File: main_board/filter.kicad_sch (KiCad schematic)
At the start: 1 part

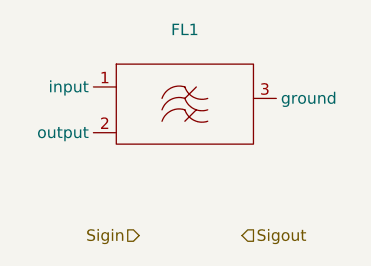
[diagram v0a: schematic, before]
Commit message: Revert "created band pass filter symbol and circuit."
This reverts commit e2b2576e5cedd48076742566f8c9abdfc840a111.

Remove bad commit
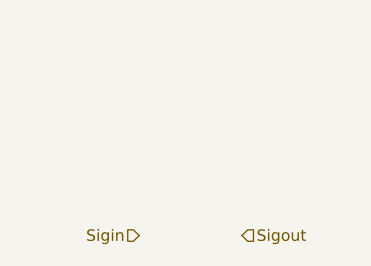
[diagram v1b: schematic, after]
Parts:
- removed FL1: ~, symbol bp_filter:457k_bandpass_filter
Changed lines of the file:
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@@
-		)
-	)
-	(symbol
-		(lib_id "bp_filter:457k_bandpass_filter")
-		(at 48.26 99.06 0)
-		(unit 1)
-		(exclude_from_sim no)
-		(in_bom yes)
-		(on_board yes)
-		(dnp no)
-		(fields_autoplaced yes)
-		(property "Reference" "FL1"
-			(at 48.26 85.09 0)
-			(effects
-				(font
-					(size 1.27 1.27)
-				)
-			)
-		)
-		(property "Value" "~"
-			(at 48.26 87.63 0)
-			(effects
-				(font
-					(size 1.27 1.27)
-				)
-			)
-		)
-		(property "Footprint" ""
-			(at 48.26 99.06 0)
-			(effects
-				(font
-					(size 1.27 1.27)
-				)
-				(hide yes)
-			)
-		)
-		(property "Datasheet" ""
-			(at 48.26 99.06 0)
-			(effects
-				(font
-					(size 1.27 1.27)
-				)
-				(hide yes)
-			)
-		)
-		(property "Description" ""
-			(at 48.26 99.06 0)
-			(effects
-				(font
-					(size 1.27 1.27)
-				)
-				(hide yes)
-			)
-		)
-		(pin "1"
-		)
-		(pin "2"
-		)
-		(pin "3"
-		)
-		(instances
-			(project ""
-				(path "/f3e20914-54f5-4568-9f0b-8875d87df3fb/4b72c036-9d03-4219-91da-5718aacb6260"
-					(reference "FL1")
-					(unit 1)
-				)
-			)
 		)
 	)

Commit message: created band pass filter symbol and circuit.
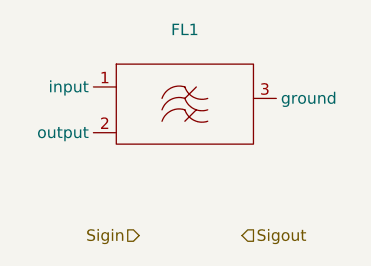
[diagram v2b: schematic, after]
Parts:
- added FL1: ~, symbol bp_filter:457k_bandpass_filter
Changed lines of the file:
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@@
+		)
+	)
+	(symbol
+		(lib_id "bp_filter:457k_bandpass_filter")
+		(at 48.26 99.06 0)
+		(unit 1)
+		(exclude_from_sim no)
+		(in_bom yes)
+		(on_board yes)
+		(dnp no)
+		(fields_autoplaced yes)
+		(property "Reference" "FL1"
+			(at 48.26 85.09 0)
+			(effects
+				(font
+					(size 1.27 1.27)
+				)
+			)
+		)
+		(property "Value" "~"
+			(at 48.26 87.63 0)
+			(effects
+				(font
+					(size 1.27 1.27)
+				)
+			)
+		)
+		(property "Footprint" ""
+			(at 48.26 99.06 0)
+			(effects
+				(font
+					(size 1.27 1.27)
+				)
+				(hide yes)
+			)
+		)
+		(property "Datasheet" ""
+			(at 48.26 99.06 0)
+			(effects
+				(font
+					(size 1.27 1.27)
+				)
+				(hide yes)
+			)
+		)
+		(property "Description" ""
+			(at 48.26 99.06 0)
+			(effects
+				(font
+					(size 1.27 1.27)
+				)
+				(hide yes)
+			)
+		)
+		(pin "1"
+		)
+		(pin "2"
+		)
+		(pin "3"
+		)
+		(instances
+			(project ""
+				(path "/f3e20914-54f5-4568-9f0b-8875d87df3fb/4b72c036-9d03-4219-91da-5718aacb6260"
+					(reference "FL1")
+					(unit 1)
+				)
+			)
 		)
 	)
